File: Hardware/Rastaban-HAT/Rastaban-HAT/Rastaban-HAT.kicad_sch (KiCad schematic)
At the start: 59 parts, among them IC1 P82B96TD,118, J1 Screw_Terminal_01x04, J10 GPIO, J11 Conn_01x06_Male, J2 Screw_Terminal_01x04, J3 Screw_Terminal_01x04, J4 Screw_Terminal_01x02, J5 Jack-DC 12V+, J6 SM04B-SRSS-TB(LF)(SN), J7 Screw_Terminal_01x02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

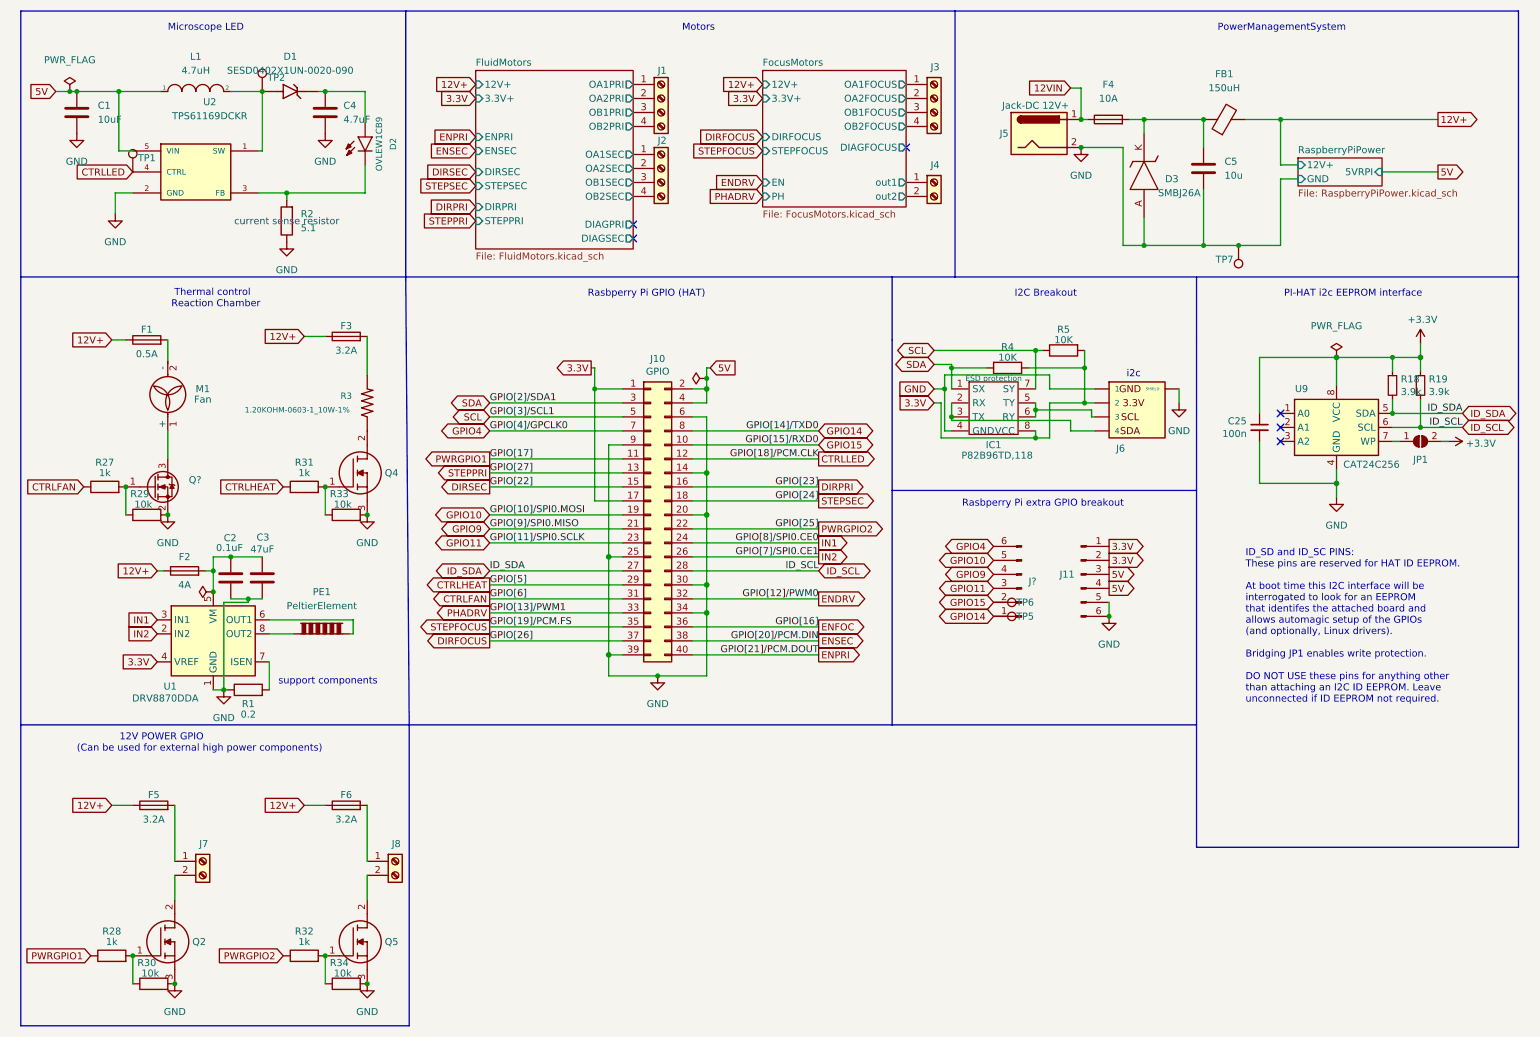
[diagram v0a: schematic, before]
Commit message: added new POLOLU DRV8838 schematic and enh main
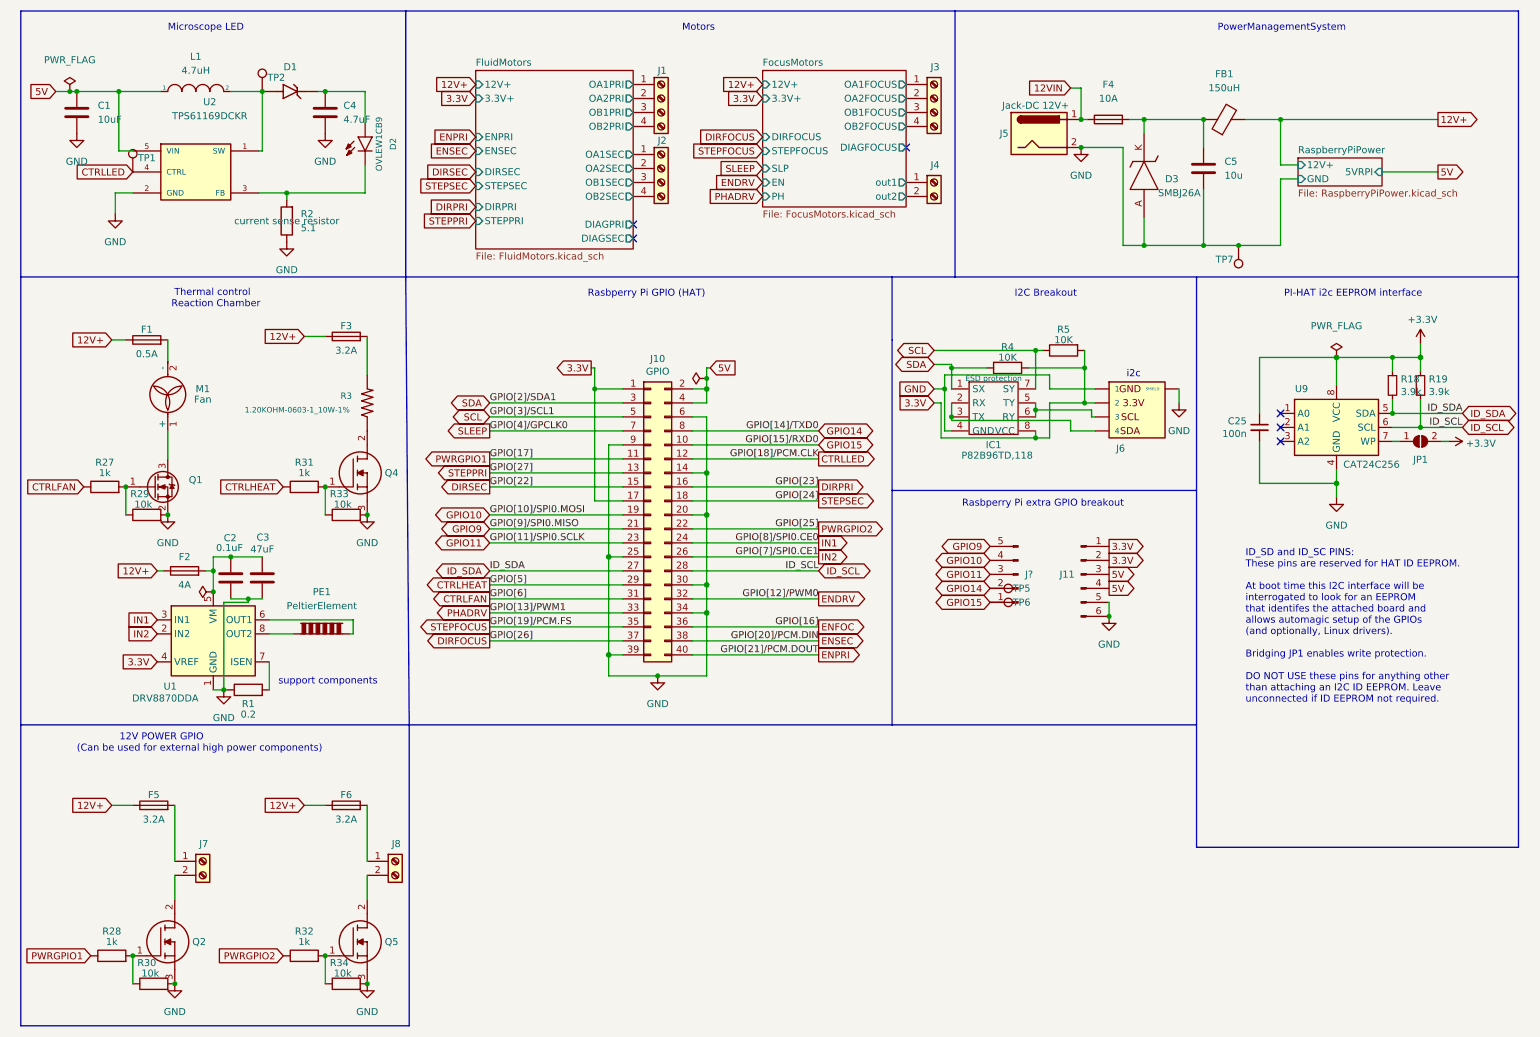
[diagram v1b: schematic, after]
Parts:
- removed J?: Conn_01x06_Male, symbol Connector:Conn_01x06_Male
- added J?: Conn_01x05_Male, symbol Connector:Conn_01x05_Male
- gave numbers to parts that had none: 1
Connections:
- net GPIO10: now also J?.4 (Pin_4)
- net GPIO11: now also J?.3 (Pin_3)
- net GPIO14: now also J?.2 (Pin_2)
- net GPIO15: now also J?.1 (Pin_1)
- net GPIO9: now also J?.5 (Pin_5)
- net GPIO4 renamed SLEEP
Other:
- sheet FocusMotors ports: added SLP; removed none
- moved on the sheet: TP5, TP6

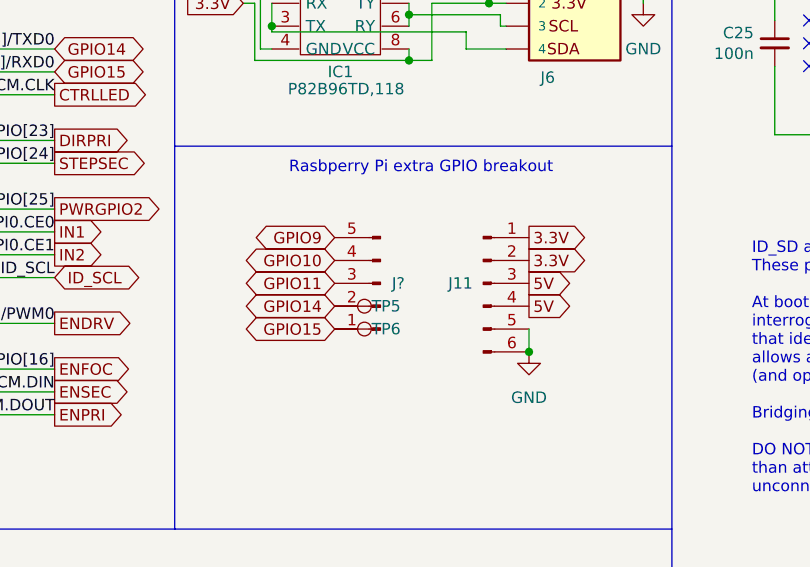
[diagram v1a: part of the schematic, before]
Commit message: updated some names on symbols
stepper motor drivers
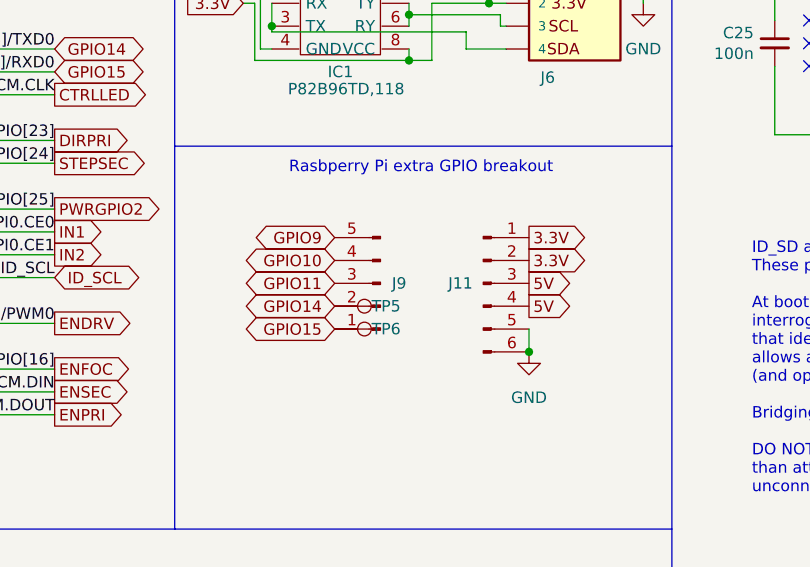
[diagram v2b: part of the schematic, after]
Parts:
- gave numbers to parts that had none: 1
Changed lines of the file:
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@@
   (symbol (lib_id "Connector:Conn_01x05_Male") (at 193.675 114.935 180) (unit 1)
     (in_bom yes) (on_board yes) (fields_autoplaced)
-    (property "Reference" "J?" (id 0) (at 194.945 114.9349 0)
+    (property "Reference" "J9" (id 0) (at 194.945 114.9349 0)
       (effects (font (size 1.27 1.27)) (justify right))
     )
@@
       (reference "J8") (unit 1) (value "Screw_Terminal_01x02") (footprint "TerminalBlock:TerminalBlock_Altech_AK300-2_P5.00mm")
     )
+    (path "/24bb24ca-3d2a-479f-b9a0-a9d8fbfb368d"
+      (reference "J9") (unit 1) (value "Conn_01x05_Male") (footprint "")
+    )
     (path "/cdd25cd5-3c1d-4ee9-8209-d2eb21ea0541"
       (reference "J10") (unit 1) (value "GPIO") (footprint "Connector_PinSocket_2.54mm:PinSocket_2x20_P2.54mm_Vertical")
@@
       (reference "J11") (unit 1) (value "Conn_01x06_Male") (footprint "Connector_PinSocket_2.54mm:PinSocket_1x06_P2.54mm_Vertical")
     )
-    (path "/24bb24ca-3d2a-479f-b9a0-a9d8fbfb368d"
-      (reference "J?") (unit 1) (value "Conn_01x05_Male") (footprint "")
-    )
     (path "/d76e85fc-4f2e-4d54-b404-7aa3a9abd669"
       (reference "JP1") (unit 1) (value "ID_WP") (footprint "Jumper:SolderJumper-2_P1.3mm_Open_RoundedPad1.0x1.5mm")
@@
     )
     (path "/509754cd-dbf1-46e6-965c-38d41c0b6924/c1dc1b77-ffa7-4f69-878e-c9530094aabf"
-      (reference "U3") (unit 1) (value "TMC2208_SILENTSTEPSTICK") (footprint "Footprints:TMC2208_SILENTSTEPSTICK")
+      (reference "U3") (unit 1) (value "TMC2208_Carrier") (footprint "Footprints:TMC2208_SILENTSTEPSTICK")
     )
     (path "/509754cd-dbf1-46e6-965c-38d41c0b6924/07c85e68-0bf7-427d-95a2-4df276793fef"
-      (reference "U4") (unit 1) (value "TMC2208_SILENTSTEPSTICK") (footprint "Footprints:TMC2208_SILENTSTEPSTICK")
+      (reference "U4") (unit 1) (value "TMC2208_Carrier") (footprint "Footprints:TMC2208_SILENTSTEPSTICK")
     )
     (path "/6c4087b1-d585-4615-84b3-d395a8b5856d/ac0fbcf0-97bf-4099-a5f5-25c63eb93075"
@@
     )
     (path "/7b03732c-6b0a-482e-b8e3-ced6ad7436b5/172503d1-ddd9-46cd-8151-cd5fd3ec266e"
-      (reference "U6") (unit 1) (value "TMC2208_SILENTSTEPSTICK") (footprint "Footprints:TMC2208_SILENTSTEPSTICK")
+      (reference "U6") (unit 1) (value "TMC2208_Carrier") (footprint "Footprints:TMC2208_SILENTSTEPSTICK")
+    )
+    (path "/7b03732c-6b0a-482e-b8e3-ced6ad7436b5/1d3758c9-7eb3-42ba-8ec8-545ede1e6fd7"
+      (reference "U7") (unit 1) (value "DRV8838 POLOLU") (footprint "Package_SON:WSON-8-1EP_2x2mm_P0.5mm_EP0.9x1.6mm")
     )
     (path "/7b03732c-6b0a-482e-b8e3-ced6ad7436b5/4618c428-5a77-4793-bb70-4e68ce6d6c82"
@@
       (reference "U9") (unit 1) (value "CAT24C256") (footprint "Footprints:SOIC127P600X175-8N")
     )
-    (path "/7b03732c-6b0a-482e-b8e3-ced6ad7436b5/1d3758c9-7eb3-42ba-8ec8-545ede1e6fd7"
-      (reference "U?") (unit 1) (value "DRV8838 POLOLU") (footprint "Package_SON:WSON-8-1EP_2x2mm_P0.5mm_EP0.9x1.6mm")
-    )
-  )
+  )

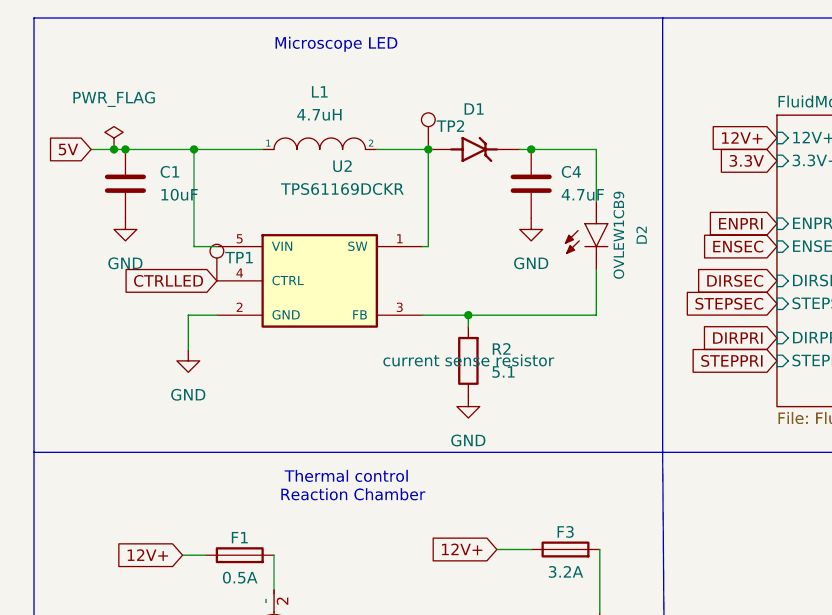
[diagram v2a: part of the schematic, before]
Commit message: Replaced old LED driver circuit with simpeler one
Advice from jeroen implemented
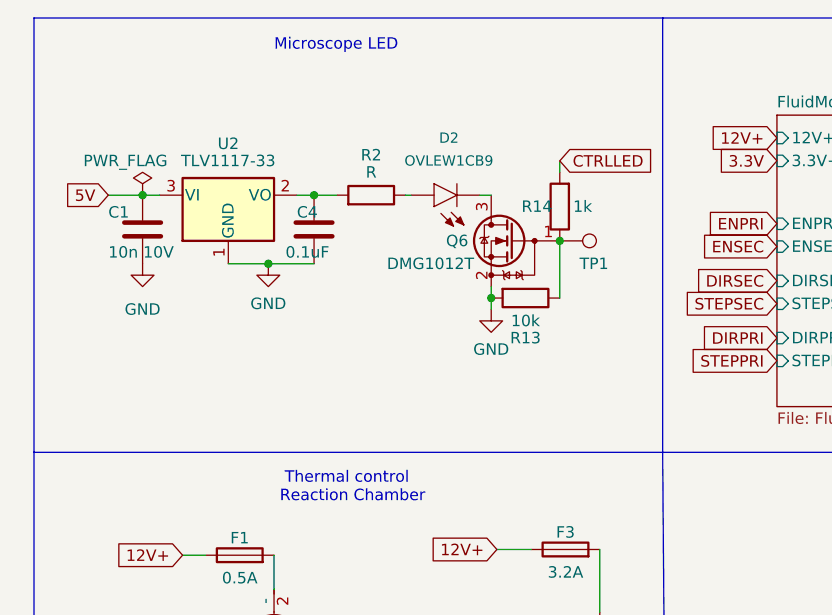
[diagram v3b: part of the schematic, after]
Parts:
- removed D1: SESD0402X1UN-0020-090, SmacSYs:SESD0402X1UN0020090, symbol SESD0402X1UN-0020-090:SESD0402X1UN-0020-090
- removed L1: 4.7uH, Inductor_SMD:L_1206_3216Metric_Pad1.22x1.90mm_HandSolder, symbol pspice:INDUCTOR
- removed TP2: TestPoint, TestPoint:TestPoint_Bridge_Pitch7.62mm_Drill1.3mm, symbol Connector:TestPoint
- removed U2: TPS61169DCKR, Snapeda:SOT65P210X110-5N, symbol TPS61169DCKR:TPS61169DCKR
- added Q6: DMG1012T, Package_TO_SOT_SMD:SOT-523, symbol Transistor_FET:DMG1012T
- added R13: 10k, Resistor_SMD:R_1206_3216Metric_Pad1.30x1.75mm_HandSolder, symbol Device:R
- added R14: 1k, Resistor_SMD:R_1206_3216Metric_Pad1.30x1.75mm_HandSolder, symbol Device:R
- added U2: TLV1117-33, symbol Regulator_Linear:TLV1117-33
- C1: value 10uF -> 10n 10V; footprint SmacSYs:SOIC127P600X175-8N -> (none)
- C4: value 4.7uF -> 0.1uF; Purpose for output ripple and loop stability -> (none)
- R2: value 5.1 -> R; footprint Resistor_SMD:R_1206_3216Metric_Pad1.30x1.75mm_HandSolder -> (none); Purpose current sense resistor -> (none)
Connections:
- net 5V: now also U2.3 (VI)
- net CTRLLED: now also R14.2; no longer TP1.1
- net GND: now also C4.1, Q6.2 (S), R13.2, U2.1 (GND); no longer C4.2, R2.1
- net at D2.A: now also R2.1; no longer C4.1
- net at R2.2: now also C4.2, U2.2 (VO); no longer D2.K (C)
- new net: Q6.1 (G), R13.1, R14.1, TP1.1
- new net: D2.K (C), Q6.3 (D)
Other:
- moved on the sheet: D2, TP1
